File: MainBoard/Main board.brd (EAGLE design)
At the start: 100 x 80 mm, 9 parts

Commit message: Update Main board.brd
Version 2
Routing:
- added copper zone on layer 1, net GND
- added copper zone on layer 16, net GND
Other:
- board size 100 x 80 mm -> 99.5 x 80 mm
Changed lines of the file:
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@@
 <setting verticaltext="up"/>
 </settings>
-<grid distance="50" unitdist="mil" unit="inch" style="dots" multiple="1" display="yes" altdistance="5" altunitdist="mil" altunit="inch"/>
+<grid distance="1" unitdist="mm" unit="mm" style="lines" multiple="1" display="yes" altdistance="0.025" altunitdist="inch" altunit="inch"/>
 <layers>
 <layer number="1" name="Top" color="4" fill="1" visible="yes" active="yes"/>
@@
 <layer number="19" name="Unrouted" color="6" fill="1" visible="yes" active="yes"/>
 <layer number="20" name="Dimension" color="24" fill="1" visible="yes" active="yes"/>
-<layer number="21" name="tPlace" color="7" fill="1" visible="yes" active="yes"/>
-<layer number="22" name="bPlace" color="7" fill="1" visible="yes" active="yes"/>
+<layer number="21" name="tPlace" color="16" fill="1" visible="yes" active="yes"/>
+<layer number="22" name="bPlace" color="16" fill="1" visible="yes" active="yes"/>
 <layer number="23" name="tOrigins" color="15" fill="1" visible="yes" active="yes"/>
 <layer number="24" name="bOrigins" color="15" fill="1" visible="yes" active="yes"/>
 <layer number="25" name="tNames" color="7" fill="1" visible="yes" active="yes"/>
-<layer number="26" name="bNames" color="7" fill="1" visible="yes" active="yes"/>
-<layer number="27" name="tValues" color="7" fill="1" visible="yes" active="yes"/>
-<layer number="28" name="bValues" color="7" fill="1" visible="yes" active="yes"/>
+<layer number="26" name="bNames" color="16" fill="1" visible="yes" active="yes"/>
+<layer number="27" name="tValues" color="16" fill="1" visible="no" active="yes"/>
+<layer number="28" name="bValues" color="16" fill="1" visible="no" active="yes"/>
 <layer number="29" name="tStop" color="7" fill="3" visible="no" active="yes"/>
 <layer number="30" name="bStop" color="7" fill="6" visible="no" active="yes"/>
@@
 <layer number="49" name="Reference" color="7" fill="1" visible="yes" active="yes"/>
 <layer number="50" name="dxf" color="7" fill="1" visible="no" active="no"/>
-<layer number="51" name="tDocu" color="7" fill="1" visible="yes" active="yes"/>
-<layer number="52" name="bDocu" color="7" fill="1" visible="yes" active="yes"/>
+<layer number="51" name="tDocu" color="16" fill="1" visible="yes" active="yes"/>
+<layer number="52" name="bDocu" color="16" fill="1" visible="yes" active="yes"/>
 <layer number="53" name="tGND_GNDA" color="7" fill="9" visible="no" active="no"/>
 <layer number="54" name="bGND_GNDA" color="1" fill="9" visible="no" active="no"/>
@@
 <board>
 <plain>
-<wire x1="0" y1="0" x2="100" y2="0" width="0" layer="20"/>
-<wire x1="100" y1="0" x2="100" y2="80" width="0" layer="20"/>
-<wire x1="100" y1="80" x2="0" y2="80" width="0" layer="20"/>
+<wire x1="0" y1="0" x2="99.54" y2="0" width="0" layer="20"/>
+<wire x1="99.54" y1="0" x2="99.54" y2="80" width="0" layer="20"/>
+<wire x1="99.54" y1="80" x2="0" y2="80" width="0" layer="20"/>
 <wire x1="0" y1="80" x2="0" y2="0" width="0" layer="20"/>
 </plain>
@@
 <wire x1="81.28" y1="20.32" x2="68.58" y2="7.62" width="0.3048" layer="16"/>
 </signal>
+<signal name="GND">
+<polygon width="0.1524" layer="1">
+<vertex x="0" y="0"/>
+<vertex x="0" y="80"/>
+<vertex x="99" y="80"/>
+<vertex x="99" y="0"/>
+</polygon>
+<polygon width="0.1524" layer="16">
+<vertex x="0" y="0"/>
+<vertex x="0" y="80"/>
+<vertex x="99" y="80"/>
+<vertex x="99" y="0"/>
+</polygon>
+</signal>
 </signals>

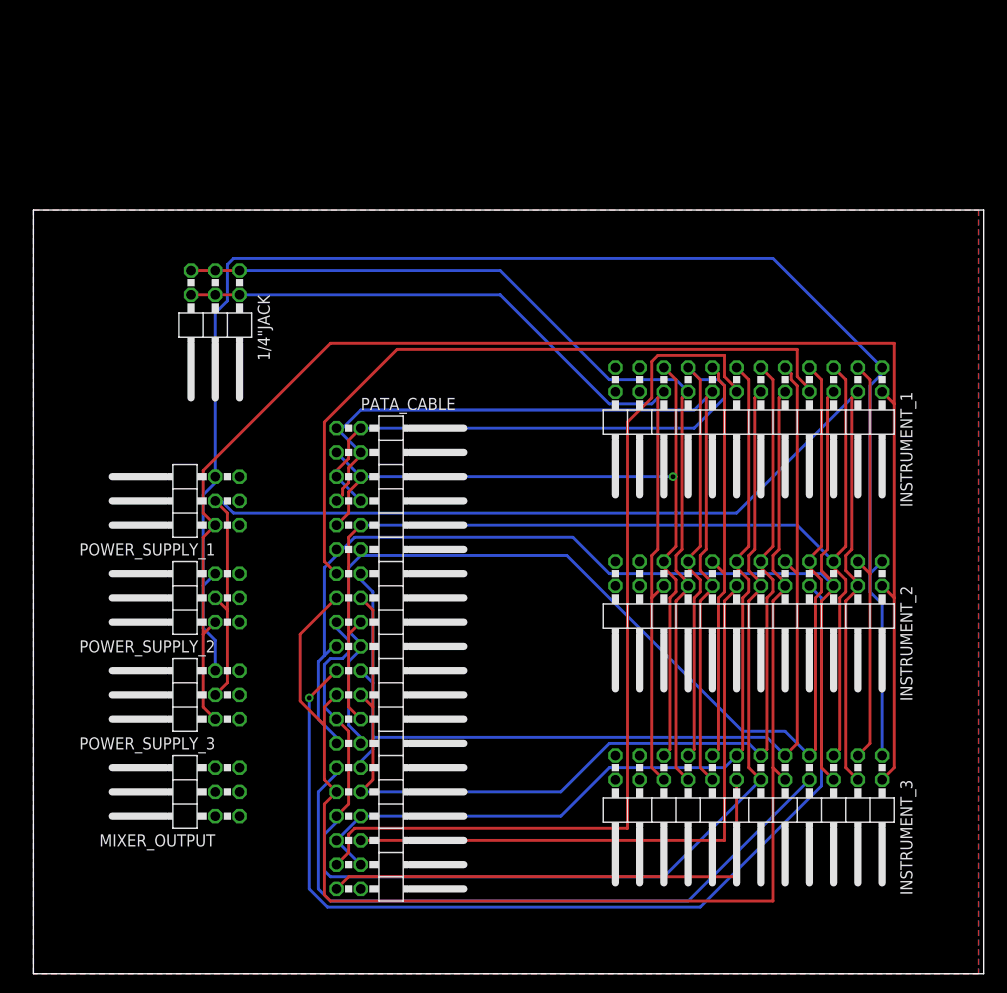
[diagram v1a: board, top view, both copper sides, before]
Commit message: Main board
Relabelled everything with power supply, labelled and redid traces.
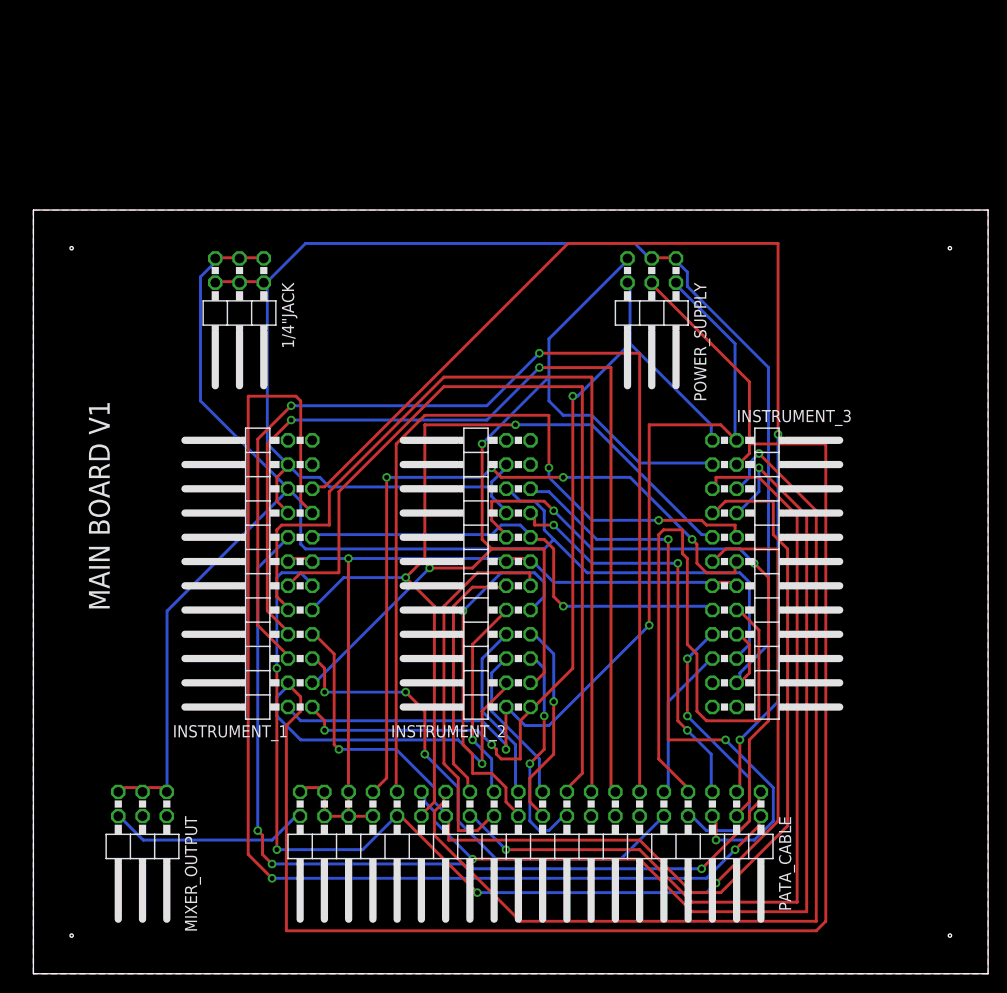
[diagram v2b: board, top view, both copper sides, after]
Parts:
- removed POWER_SUPPLY_1, POWER_SUPPLY_2, POWER_SUPPLY_3: (no value), pinhead:2X03/90
- added POWER_SUPPLY: (no value), pinhead:2X03/90
- moved INSTRUMENT_1 54.3 mm to (22.9, 41.9), turned to 90 degrees
- moved INSTRUMENT_2 29.6 mm to (45.7, 41.9), turned to 90 degrees
- moved INSTRUMENT_3 25.5 mm to (77.5, 41.9), turned to 270 degrees
- moved PATA_CABLE 24.7 mm to (52.1, 12.7), turned to 180 degrees
- moved MIXER_OUTPUT 7.41 mm to (11.4, 12.7), turned to 180 degrees
- moved 1/4"JACK 2.84 mm to (21.6, 68.6)
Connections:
- net N$3 renamed POT_20
- net N$41 renamed POT_12
- net N$45 renamed POT_4
- removed net 5V: INSTRUMENT_1.1, INSTRUMENT_2.1, INSTRUMENT_3.1, POWER_SUPPLY_1.6, POWER_SUPPLY_2.6, POWER_SUPPLY_3.6
- removed net AUDIO_OUTPUT: 1/4"JACK.2, 1/4"JACK.4, 1/4"JACK.6, INSTRUMENT_1.20, INSTRUMENT_2.20, INSTRUMENT_3.20
- removed net N$1: INSTRUMENT_2.22
- removed net N$14: INSTRUMENT_1.22
- removed net N$18: INSTRUMENT_1.14, PATA_CABLE.37
- removed net N$2: INSTRUMENT_2.14, PATA_CABLE.36
- removed net N$31: PATA_CABLE.40
- removed net N$4: INSTRUMENT_3.22
- removed net N$5: INSTRUMENT_3.14, PATA_CABLE.39
- removed net N$52: INSTRUMENT_1.23
- removed net N$53: INSTRUMENT_1.24
- removed net N$54: INSTRUMENT_2.23
- removed net N$55: INSTRUMENT_2.24
- removed net N$56: INSTRUMENT_3.23
- removed net N$57: INSTRUMENT_3.24
- removed net N$58: POWER_SUPPLY_1.1
- removed net N$59: POWER_SUPPLY_1.3
- removed net N$60: POWER_SUPPLY_1.5
- removed net N$64: POWER_SUPPLY_2.1
- removed net N$65: POWER_SUPPLY_2.3
- removed net N$66: POWER_SUPPLY_2.5
- removed net N$7: INSTRUMENT_1.21
- removed net N$70: POWER_SUPPLY_3.1
- removed net N$71: POWER_SUPPLY_3.3
- removed net N$72: POWER_SUPPLY_3.5
- removed net N$8: INSTRUMENT_2.21
- removed net PETA_CABLE: INSTRUMENT_3.21
- new net +5V: INSTRUMENT_1.1, INSTRUMENT_2.1, INSTRUMENT_3.1, POWER_SUPPLY.6
- new net ANALOG_OUTPUT: 1/4"JACK.1, 1/4"JACK.3, 1/4"JACK.5, INSTRUMENT_1.20, INSTRUMENT_2.20, INSTRUMENT_3.20, MIXER_OUTPUT.1, MIXER_OUTPUT.3, MIXER_OUTPUT.5
- new net GND: MIXER_OUTPUT.6, PATA_CABLE.40
- new net POT_1: INSTRUMENT_1.5, PATA_CABLE.10
- new net POT_10: INSTRUMENT_2.6, PATA_CABLE.19
- new net POT_11: INSTRUMENT_2.7, PATA_CABLE.20
- new net POT_13: INSTRUMENT_2.9, PATA_CABLE.22
- new net POT_14: INSTRUMENT_2.10, PATA_CABLE.23
- new net POT_15: INSTRUMENT_2.11, PATA_CABLE.24
- new net POT_16: INSTRUMENT_2.12, PATA_CABLE.25
- new net POT_2: INSTRUMENT_1.6, PATA_CABLE.11
- new net POT_3: PATA_CABLE.12
- new net POT_5: PATA_CABLE.14
- new net POT_6: INSTRUMENT_1.10, PATA_CABLE.15
- new net POT_7: PATA_CABLE.16
- new net POT_8: INSTRUMENT_1.12, PATA_CABLE.17
- new net POT_9: INSTRUMENT_2.5, PATA_CABLE.18
- new net SWITCH_4: INSTRUMENT_2.16, PATA_CABLE.4
- new net SWITCH_5: INSTRUMENT_2.17, PATA_CABLE.5
- new net SWITCH_6: INSTRUMENT_2.19, PATA_CABLE.6
- new net SWITCH_7: INSTRUMENT_3.16, PATA_CABLE.7
- new net SWITCH_8: INSTRUMENT_3.17, PATA_CABLE.8
- new net SWITCH_9: INSTRUMENT_3.19, PATA_CABLE.9
- net +12V: now also POWER_SUPPLY.2; no longer POWER_SUPPLY_1.2, POWER_SUPPLY_2.2, POWER_SUPPLY_3.2
- net -12V: now also POWER_SUPPLY.4; no longer POWER_SUPPLY_1.4, POWER_SUPPLY_2.4, POWER_SUPPLY_3.4
- net ANALOG_GND: now also 1/4"JACK.2, 1/4"JACK.4, 1/4"JACK.6, INSTRUMENT_1.22, INSTRUMENT_2.22, INSTRUMENT_3.22, POWER_SUPPLY.1, POWER_SUPPLY.3; no longer 1/4"JACK.1, 1/4"JACK.3, 1/4"JACK.5
- net DIGITAL_GND: now also POWER_SUPPLY.5
- net POT_17: no longer INSTRUMENT_1.5, INSTRUMENT_2.5, PATA_CABLE.10, PATA_CABLE.18
- net POT_18: no longer INSTRUMENT_1.6, INSTRUMENT_2.6, PATA_CABLE.11, PATA_CABLE.19
- net POT_19: no longer INSTRUMENT_2.7, PATA_CABLE.12, PATA_CABLE.20
- net POT_21: no longer INSTRUMENT_2.9, PATA_CABLE.14, PATA_CABLE.22
- net POT_22: no longer INSTRUMENT_1.10, INSTRUMENT_2.10, PATA_CABLE.15, PATA_CABLE.23
- net POT_23: no longer INSTRUMENT_2.11, PATA_CABLE.16, PATA_CABLE.24
- net POT_24: no longer INSTRUMENT_1.12, INSTRUMENT_2.12, PATA_CABLE.17, PATA_CABLE.25
- net SWITCH_1: no longer INSTRUMENT_2.16, INSTRUMENT_3.16, PATA_CABLE.4, PATA_CABLE.7
- net SWITCH_2: no longer INSTRUMENT_2.17, INSTRUMENT_3.17, PATA_CABLE.5, PATA_CABLE.8
- net SWITCH_3: no longer INSTRUMENT_2.19, INSTRUMENT_3.19, PATA_CABLE.6, PATA_CABLE.9
- net TO_POT_PCB: now also INSTRUMENT_1.14, INSTRUMENT_2.14, INSTRUMENT_3.14, PATA_CABLE.36, PATA_CABLE.37, PATA_CABLE.39
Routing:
- net 5V: track 163.0 -> 0.00 mm
- net ANALOG_OUTPUT: track 0.00 -> 149.5 mm
- net POT_2: track 0.00 -> 113.9 mm, vias 0 -> 2
- net AUDIO_OUTPUT: track 98.3 -> 0.00 mm
- net N$18: track 95.3 -> 0.00 mm
- net POT_6: track 0.00 -> 94.0 mm
- net +5V: track 0.00 -> 93.9 mm, vias 0 -> 3
- net POT_8: track 0.00 -> 87.5 mm
- net POT_12: track 105.2 -> 19.1 mm, vias 1 -> 0
- net SWITCH_7: track 0.00 -> 70.1 mm
- net N$2: track 65.3 -> 0.00 mm
- net -12V: track 139.0 -> 202.9 mm, vias 0 -> 1
- net SWITCH_6: track 0.00 -> 63.9 mm, vias 0 -> 3
- net SWITCH_4: track 0.00 -> 63.1 mm, vias 0 -> 2
- net ANALOG_GND: track 100.1 -> 161.9 mm
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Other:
- board size 99.5 x 80 mm -> 100 x 80 mm
- board text added: "MAIN BOARD V1"

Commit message: Version 2 of mainboard
Corrected lots of thingamajics.
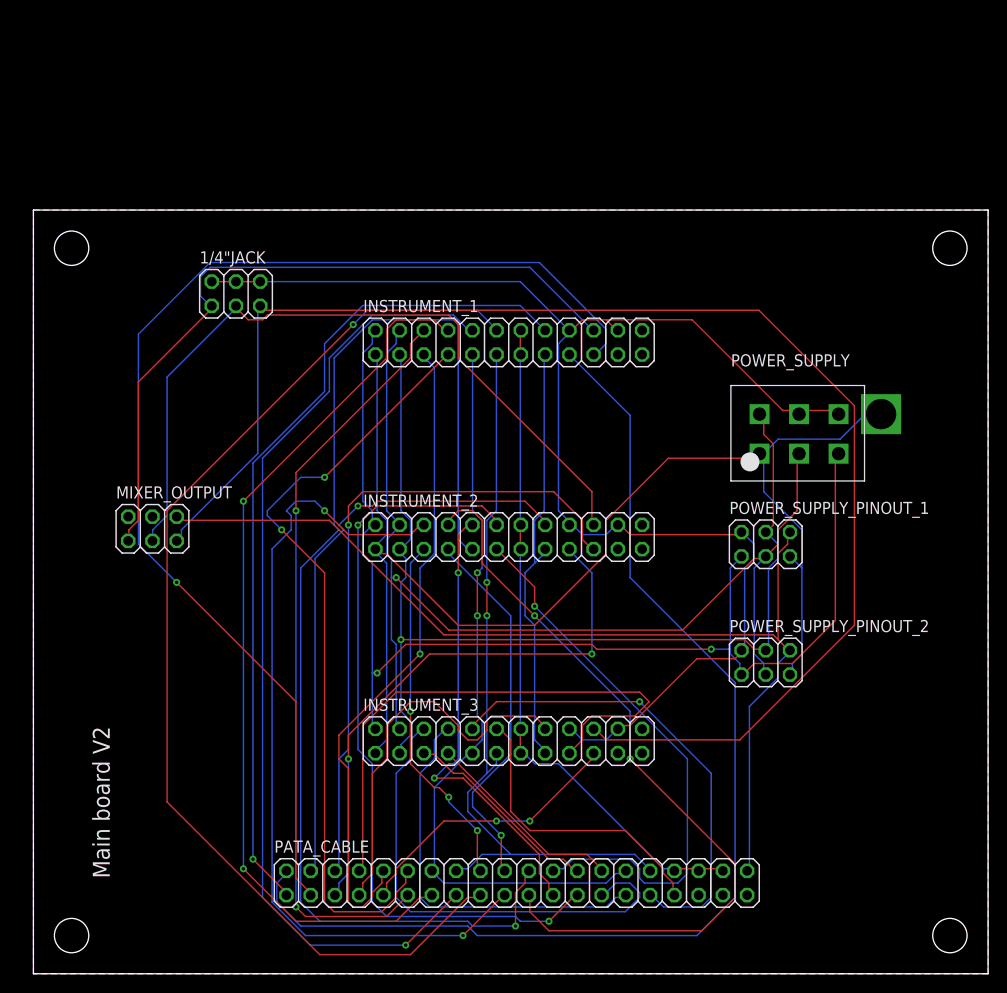
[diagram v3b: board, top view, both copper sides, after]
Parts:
- added POWER_SUPPLY_PINOUT_1, POWER_SUPPLY_PINOUT_2: (no value), pinhead:2X03
- 1/4"JACK, MIXER_OUTPUT: device pinhead:2X03/90 -> pinhead:2X03
- INSTRUMENT_1, INSTRUMENT_2, INSTRUMENT_3: device pinhead:2X12/90 -> pinhead:2X12
- PATA_CABLE: device pinhead:2X20/90 -> pinhead:2X20
- POWER_SUPPLY: value (none) -> TER6PIN_VERT; device pinhead:2X03/90 -> TE6Pin:CAPSTONE_1-770875-0
- moved INSTRUMENT_1 36.2 mm to (49.8, 66.1), turned to 0 degrees
- moved MIXER_OUTPUT 33.9 mm to (12.5, 46.6), turned to 0 degrees
- moved INSTRUMENT_3 32.8 mm to (49.8, 24.4), turned to 0 degrees
- moved POWER_SUPPLY 15.1 mm to (76.1, 58.6), turned to 0 degrees
- moved INSTRUMENT_2 5.60 mm to (49.8, 45.8), turned to 0 degrees
- moved PATA_CABLE 3.50 mm to (50.6, 9.51), turned to 0 degrees
- moved 1/4"JACK 2.68 mm to (21.2, 71.2), turned to 0 degrees
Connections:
- net POT_1 renamed POT_1A
- net POT_10 renamed POT_5B
- net POT_11 renamed POT_6A
- net POT_12 renamed POT_6B
- net POT_13 renamed POT_7A
- net POT_14 renamed POT_7B
- net POT_15 renamed POT_8A
- net POT_16 renamed POT_8B
- net POT_17 renamed POT_9A
- net POT_18 renamed POT_9B
- net POT_2 renamed POT_1B
- net POT_20 renamed POT_10B
- net POT_22 renamed POT_11B
- net POT_24 renamed POT_12B
- net POT_4 renamed POT_2B
- net POT_6 renamed POT_3B
- net POT_8 renamed POT_4B
- net POT_9 renamed POT_5A
- removed net ANALOG_OUTPUT: 1/4"JACK.1, 1/4"JACK.3, 1/4"JACK.5, INSTRUMENT_1.20, INSTRUMENT_2.20, INSTRUMENT_3.20, MIXER_OUTPUT.1, MIXER_OUTPUT.3, MIXER_OUTPUT.5
- removed net POT_19: INSTRUMENT_1.7, INSTRUMENT_3.7, PATA_CABLE.28
- removed net POT_21: INSTRUMENT_1.9, INSTRUMENT_3.9, PATA_CABLE.30
- removed net POT_23: INSTRUMENT_1.11, INSTRUMENT_3.11, PATA_CABLE.32
- removed net POT_3: PATA_CABLE.12
- removed net POT_5: PATA_CABLE.14
- removed net POT_7: PATA_CABLE.16
- new net ANALOG_OUTPUT_1: 1/4"JACK.1, INSTRUMENT_1.20, MIXER_OUTPUT.1
- new net ANALOG_OUTPUT_2: 1/4"JACK.3, INSTRUMENT_2.20, MIXER_OUTPUT.3
- new net ANALOG_OUTPUT_3: 1/4"JACK.5, INSTRUMENT_3.20, MIXER_OUTPUT.5
- new net POT_10A: INSTRUMENT_3.7, PATA_CABLE.28
- new net POT_11A: INSTRUMENT_1.9, INSTRUMENT_3.9, PATA_CABLE.14, PATA_CABLE.30
- new net POT_12A: INSTRUMENT_1.11, INSTRUMENT_3.11, PATA_CABLE.16, PATA_CABLE.32
- new net POT_2A: INSTRUMENT_1.7, PATA_CABLE.12
- net +12V: now also POWER_SUPPLY.+12V, POWER_SUPPLY_PINOUT_1.1, POWER_SUPPLY_PINOUT_2.1; no longer POWER_SUPPLY.2
- net +5V: now also POWER_SUPPLY.+5V, POWER_SUPPLY.NULL, POWER_SUPPLY_PINOUT_1.5, POWER_SUPPLY_PINOUT_2.5; no longer POWER_SUPPLY.6
- net -12V: now also POWER_SUPPLY.-12V, POWER_SUPPLY_PINOUT_1.3, POWER_SUPPLY_PINOUT_2.3; no longer POWER_SUPPLY.4
- net ANALOG_GND: now also POWER_SUPPLY.AGND0, POWER_SUPPLY.AGND1, POWER_SUPPLY_PINOUT_1.2, POWER_SUPPLY_PINOUT_2.2; no longer POWER_SUPPLY.1, POWER_SUPPLY.3
- net DIGITAL_GND: now also POWER_SUPPLY.DGND, POWER_SUPPLY_PINOUT_1.4, POWER_SUPPLY_PINOUT_2.4; no longer POWER_SUPPLY.5
- net GND: now also POWER_SUPPLY_PINOUT_1.6, POWER_SUPPLY_PINOUT_2.6
- net TO_POT_PCB: no longer PATA_CABLE.35, PATA_CABLE.37, PATA_CABLE.39
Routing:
- net ANALOG_OUTPUT_3: track 0.00 -> 150.8 mm
- net ANALOG_OUTPUT: track 149.5 -> 0.00 mm
- net POT_23: track 129.3 -> 0.00 mm, vias 4 -> 0
- net POT_19: track 113.4 -> 0.00 mm, vias 1 -> 0
- net POT_21: track 89.9 -> 0.00 mm, vias 2 -> 0
- net POT_7A: track 39.1 -> 128.1 mm
- net -12V: track 202.9 -> 114.4 mm
- net GND: track 21.1 -> 106.7 mm
- net POT_2A: track 0.00 -> 81.0 mm, vias 0 -> 2
- net POT_12A: track 0.00 -> 79.8 mm, vias 0 -> 2
- net ANALOG_OUTPUT_2: track 0.00 -> 79.6 mm
- net POT_11A: track 0.00 -> 78.8 mm, vias 0 -> 2
- net ANALOG_OUTPUT_1: track 0.00 -> 76.1 mm
- net POT_5B: track 16.8 -> 86.3 mm, vias 0 -> 2
- net POT_9A: track 90.1 -> 21.1 mm, vias 1 -> 0
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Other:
- board text added: "Main board V2"
- board text removed: "MAIN BOARD V1"
